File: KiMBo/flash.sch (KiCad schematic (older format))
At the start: 31 parts, among them IC1 24LC32AT-I/OT, U1 OSD3358, U5 74LVC1G06, U6 EMMC**G-S100

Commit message: More footprint association
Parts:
- IC1: footprint (none) -> TO_SOT_Packages_SMD:SOT-23-5
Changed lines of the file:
@@
 Connection ~ 12800 2650
 $Comp
-L GND #PWR092
+L GND #PWR093
 U 1 1 5893C2D6
 P 8300 4850
-F 0 "#PWR092" H 8300 4600 50  0001 C CNN
+F 0 "#PWR093" H 8300 4600 50  0001 C CNN
 F 1 "GND" H 8305 4677 50  0000 C CNN
 F 2 "" H 8300 4850 50  0000 C CNN
@@
 F 0 "IC1" H 12250 7018 50  0000 C CNN
 F 1 "24LC32AT-I/OT" H 12250 6927 50  0000 C CNN
-F 2 "" H 12250 6836 50  0001 C CIN
+F 2 "TO_SOT_Packages_SMD:SOT-23-5" H 12250 6836 50  0001 C CIN
 F 3 "" H 12250 6400 50  0000 C CNN
 	1    12250 6400
@@
 	11400 7000 11400 6950
 $Comp
-L GND #PWR093
+L GND #PWR094
 U 1 1 589CAA98
 P 12250 7050
-F 0 "#PWR093" H 12250 6800 50  0001 C CNN
+F 0 "#PWR094" H 12250 6800 50  0001 C CNN
 F 1 "GND" H 12255 6877 50  0000 C CNN
 F 2 "" H 12250 7050 50  0000 C CNN
@@
 $EndComp
 $Comp
-L GND #PWR094
+L GND #PWR095
 U 1 1 58ED63A5
 P 6750 7550
-F 0 "#PWR094" H 6750 7300 50  0001 C CNN
+F 0 "#PWR095" H 6750 7300 50  0001 C CNN
 F 1 "GND" H 6755 7377 50  0000 C CNN
 F 2 "" H 6750 7550 50  0000 C CNN
@@
 $EndComp
 $Comp
-L GND #PWR095
+L GND #PWR096
 U 1 1 58ED63B8
 P 6950 6900
-F 0 "#PWR095" H 6950 6650 50  0001 C CNN
+F 0 "#PWR096" H 6950 6650 50  0001 C CNN
 F 1 "GND" H 6955 6727 50  0000 C CNN
 F 2 "" H 6950 6900 50  0000 C CNN
@@
 $EndComp
 $Comp
-L GND #PWR096
+L GND #PWR097
 U 1 1 58ED63D4
 P 6450 8550
-F 0 "#PWR096" H 6450 8300 50  0001 C CNN
+F 0 "#PWR097" H 6450 8300 50  0001 C CNN
 F 1 "GND" H 6455 8377 50  0000 C CNN
 F 2 "" H 6450 8550 50  0000 C CNN
@@
 SERVO_0
 $Comp
-L VDD_3V3B #PWR097
+L VDD_3V3B #PWR098
 U 1 1 59E9BAE0
 P 10550 2600
-F 0 "#PWR097" H 10550 2450 50  0001 C CNN
+F 0 "#PWR098" H 10550 2450 50  0001 C CNN
 F 1 "VDD_3V3B" H 10565 2773 50  0000 C CNN
 F 2 "" H 10550 2600 50  0000 C CNN
@@
 USR0
 $Comp
-L VDD_3V3B #PWR098
+L VDD_3V3B #PWR099
 U 1 1 59FAFB00
 P 6450 8100
-F 0 "#PWR098" H 6450 7950 50  0001 C CNN
+F 0 "#PWR099" H 6450 7950 50  0001 C CNN
 F 1 "VDD_3V3B" H 6465 8273 50  0000 C CNN
 F 2 "" H 6450 8100 50  0000 C CNN
@@
 $EndComp
 $Comp
-L VDD_3V3B #PWR099
+L VDD_3V3B #PWR0100
 U 1 1 59FBC4DE
 P 6750 6450
-F 0 "#PWR099" H 6750 6300 50  0001 C CNN
+F 0 "#PWR0100" H 6750 6300 50  0001 C CNN
 F 1 "VDD_3V3B" H 6765 6623 50  0000 C CNN
 F 2 "" H 6750 6450 50  0000 C CNN
@@
 Connection ~ 11400 6600
 $Comp
-L VDD_3V3B #PWR0100
+L VDD_3V3B #PWR0101
 U 1 1 59FBD7EE
 P 11400 5950
-F 0 "#PWR0100" H 11400 5800 50  0001 C CNN
+F 0 "#PWR0101" H 11400 5800 50  0001 C CNN
 F 1 "VDD_3V3B" H 11415 6123 50  0000 C CNN
 F 2 "" H 11400 5950 50  0000 C CNN

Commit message: Create more footprints and add more associations
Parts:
- OSC1: footprint (none) -> KiMBo:Crystal_SMD_ASDMB_4Pads
- TP5: footprint (none) -> Measurement_Points:Measurement_Point_Round-SMD-Pad_Small
- U5: footprint (none) -> TO_SOT_Packages_SMD:SC-70-5
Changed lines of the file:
@@
 F 0 "U5" H 6450 7350 50  0000 L CNN
 F 1 "74LVC1G06" H 6800 7100 50  0000 L CNN
-F 2 "" H 6750 7200 50  0001 C CNN
+F 2 "TO_SOT_Packages_SMD:SC-70-5" H 6750 7200 50  0001 C CNN
 F 3 "" H 6750 7200 50  0000 C CNN
 	1    6750 7200
@@
 F 0 "OSC1" H 7050 8550 60  0000 C CNN
 F 1 "ASDMB" H 7050 8100 60  0000 C CNN
-F 2 "" H 7090 8260 60  0001 C CNN
+F 2 "KiMBo:Crystal_SMD_ASDMB_4Pads" H 7090 8260 60  0001 C CNN
 F 3 "" H 7090 8260 60  0001 C CNN
 	1    7050 8300
@@
 F 0 "TP5" H 11750 6750 50  0000 L CNN
 F 1 "Test_Point" H 11858 6579 50  0001 L CNN
-F 2 "" H 12000 6550 50  0001 C CNN
+F 2 "Measurement_Points:Measurement_Point_Round-SMD-Pad_Small" H 12000 6550 50  0001 C CNN
 F 3 "" H 12000 6550 50  0000 C CNN
 	1    11800 6550

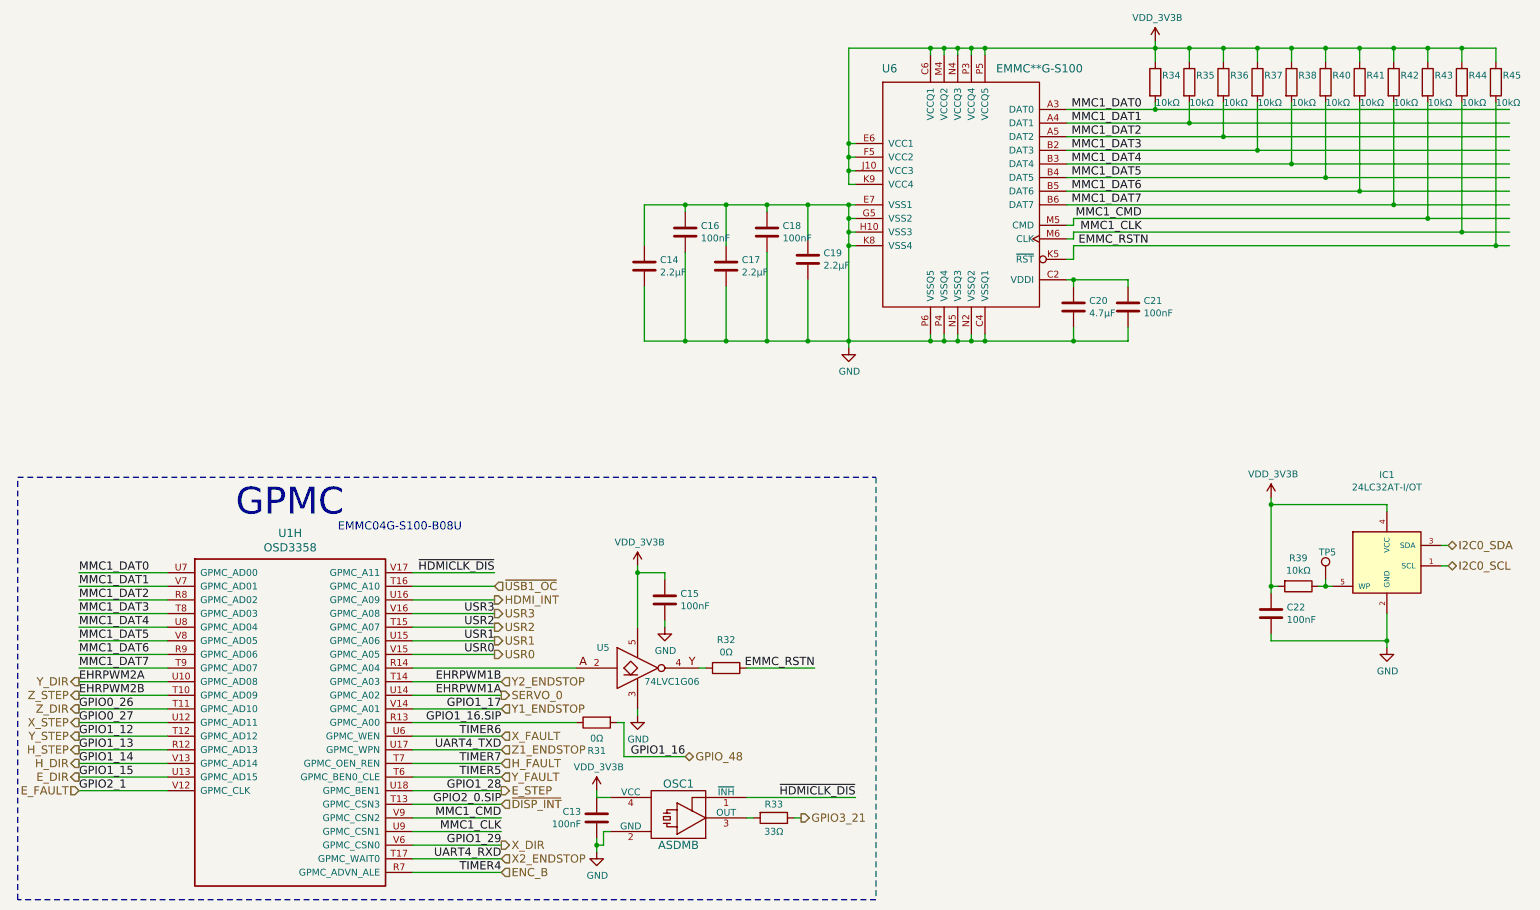
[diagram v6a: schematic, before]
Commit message: Begin layout
Arrange all connectors to get a feel for the area.
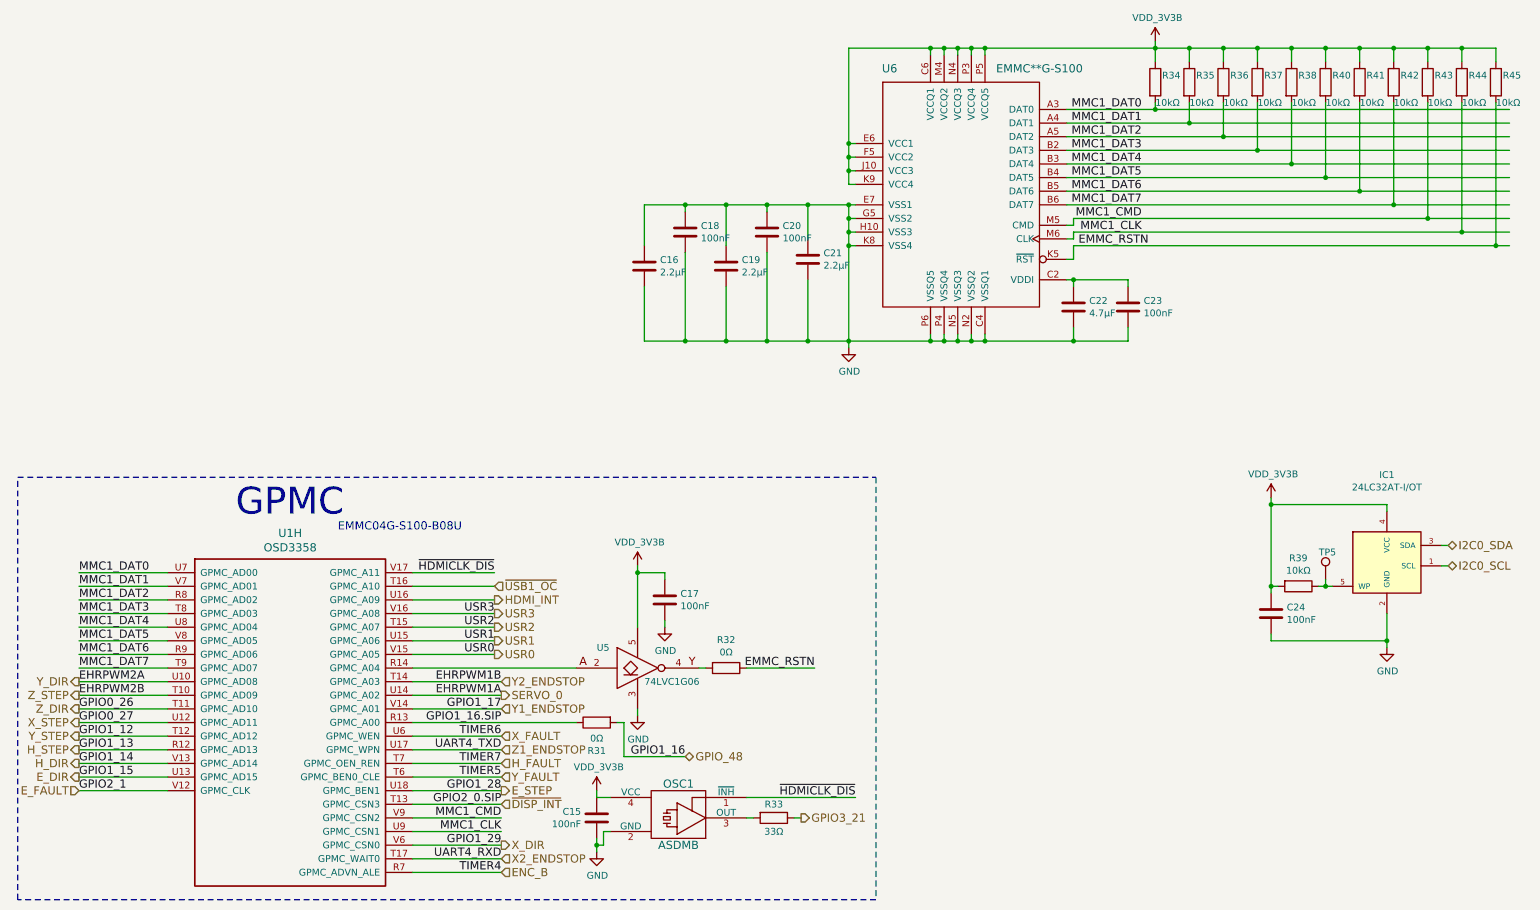
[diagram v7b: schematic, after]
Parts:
- renumbered C13 to C15, C14 to C16, C15 to C17, C16 to C18, C17 to C19, C18 to C20, C19 to C21, C20 to C22, C21 to C23, C22 to C24
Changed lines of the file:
@@
 Connection ~ 12800 2650
 $Comp
-L GND #PWR093
+L GND #PWR096
 U 1 1 5893C2D6
 P 8300 4850
-F 0 "#PWR093" H 8300 4600 50  0001 C CNN
+F 0 "#PWR096" H 8300 4600 50  0001 C CNN
 F 1 "GND" H 8305 4677 50  0000 C CNN
 F 2 "" H 8300 4850 50  0000 C CNN
@@
 Connection ~ 8300 4800
 $Comp
-L C C20
+L C C22
 U 1 1 5893CB56
 P 9950 4550
-F 0 "C20" H 10065 4596 50  0000 L CNN
+F 0 "C22" H 10065 4596 50  0000 L CNN
 F 1 "4.7μF" H 10065 4505 50  0000 L CNN
 F 2 "Capacitors_SMD:C_0805" H 9950 4550 50  0001 C CNN
@@
 $EndComp
 $Comp
-L C C21
+L C C23
 U 1 1 5893CB95
 P 10350 4550
-F 0 "C21" H 10465 4596 50  0000 L CNN
+F 0 "C23" H 10465 4596 50  0000 L CNN
 F 1 "100nF" H 10465 4505 50  0000 L CNN
 F 2 "Capacitors_SMD:C_0603" H 10350 4550 50  0001 C CNN
@@
 Connection ~ 9950 4350
 $Comp
-L C C19
+L C C21
 U 1 1 5893CF89
 P 8000 4200
-F 0 "C19" H 8115 4246 50  0000 L CNN
+F 0 "C21" H 8115 4246 50  0000 L CNN
 F 1 "2.2μF" H 8115 4155 50  0000 L CNN
 F 2 "Capacitors_SMD:C_0805" H 8000 4200 50  0001 C CNN
@@
 $EndComp
 $Comp
-L C C18
+L C C20
 U 1 1 5893D253
 P 7700 4000
-F 0 "C18" H 7815 4046 50  0000 L CNN
+F 0 "C20" H 7815 4046 50  0000 L CNN
 F 1 "100nF" H 7815 3955 50  0000 L CNN
 F 2 "Capacitors_SMD:C_0603" H 7700 4000 50  0001 C CNN
@@
 $EndComp
 $Comp
-L C C17
+L C C19
 U 1 1 5893D333
 P 7400 4250
-F 0 "C17" H 7515 4296 50  0000 L CNN
+F 0 "C19" H 7515 4296 50  0000 L CNN
 F 1 "2.2μF" H 7515 4205 50  0000 L CNN
 F 2 "Capacitors_SMD:C_0805" H 7400 4250 50  0001 C CNN
@@
 $EndComp
 $Comp
-L C C16
+L C C18
 U 1 1 5893D48C
 P 7100 4000
-F 0 "C16" H 7215 4046 50  0000 L CNN
+F 0 "C18" H 7215 4046 50  0000 L CNN
 F 1 "100nF" H 7215 3955 50  0000 L CNN
 F 2 "Capacitors_SMD:C_0603" H 7100 4000 50  0001 C CNN
@@
 $EndComp
 $Comp
-L C C14
+L C C16
 U 1 1 5893D4EE
 P 6800 4250
-F 0 "C14" H 6915 4296 50  0000 L CNN
+F 0 "C16" H 6915 4296 50  0000 L CNN
 F 1 "2.2μF" H 6915 4205 50  0000 L CNN
 F 2 "Capacitors_SMD:C_0805" H 6800 4250 50  0001 C CNN
@@
 	11400 6600 11450 6600
 $Comp
-L C C22
+L C C24
 U 1 1 589CA9AC
 P 11400 6800
-F 0 "C22" H 11515 6846 50  0000 L CNN
+F 0 "C24" H 11515 6846 50  0000 L CNN
 F 1 "100nF" H 11515 6755 50  0000 L CNN
 F 2 "Capacitors_SMD:C_0603" H 11400 6800 50  0001 C CNN
@@
 	11400 7000 11400 6950
 $Comp
-L GND #PWR094
+L GND #PWR097
 U 1 1 589CAA98
 P 12250 7050
-F 0 "#PWR094" H 12250 6800 50  0001 C CNN
+F 0 "#PWR097" H 12250 6800 50  0001 C CNN
 F 1 "GND" H 12255 6877 50  0000 C CNN
 F 2 "" H 12250 7050 50  0000 C CNN
@@
 $EndComp
 $Comp
-L GND #PWR095
+L GND #PWR098
 U 1 1 58ED63A5
 P 6750 7550
-F 0 "#PWR095" H 6750 7300 50  0001 C CNN
+F 0 "#PWR098" H 6750 7300 50  0001 C CNN
 F 1 "GND" H 6755 7377 50  0000 C CNN
 F 2 "" H 6750 7550 50  0000 C CNN
@@
 $EndComp
 $Comp
-L C C15
+L C C17
 U 1 1 58ED63B1
 P 6950 6700
-F 0 "C15" H 7065 6746 50  0000 L CNN
+F 0 "C17" H 7065 6746 50  0000 L CNN
 F 1 "100nF" H 7065 6655 50  0000 L CNN
 F 2 "Capacitors_SMD:C_0603" H 6988 6550 50  0001 C CNN
@@
 $EndComp
 $Comp
-L GND #PWR096
+L GND #PWR099
 U 1 1 58ED63B8
 P 6950 6900
-F 0 "#PWR096" H 6950 6650 50  0001 C CNN
+F 0 "#PWR099" H 6950 6650 50  0001 C CNN
 F 1 "GND" H 6955 6727 50  0000 C CNN
 F 2 "" H 6950 6900 50  0000 C CNN
@@
 $EndComp
 $Comp
-L C C13
+L C C15
 U 1 1 58ED63CD
 P 6450 8300
-F 0 "C13" H 6565 8346 50  0000 L CNN
+F 0 "C15" H 6565 8346 50  0000 L CNN
 F 1 "100nF" H 6565 8255 50  0000 L CNN
 F 2 "Capacitors_SMD:C_0603" H 6450 8300 50  0001 C CNN
@@
 $EndComp
 $Comp
-L GND #PWR097
+L GND #PWR0100
 U 1 1 58ED63D4
 P 6450 8550
-F 0 "#PWR097" H 6450 8300 50  0001 C CNN
+F 0 "#PWR0100" H 6450 8300 50  0001 C CNN
 F 1 "GND" H 6455 8377 50  0000 C CNN
 F 2 "" H 6450 8550 50  0000 C CNN
@@
 SERVO_0
 $Comp
-L VDD_3V3B #PWR098
+L VDD_3V3B #PWR0101
 U 1 1 59E9BAE0
 P 10550 2600
-F 0 "#PWR098" H 10550 2450 50  0001 C CNN
+F 0 "#PWR0101" H 10550 2450 50  0001 C CNN
 F 1 "VDD_3V3B" H 10565 2773 50  0000 C CNN
 F 2 "" H 10550 2600 50  0000 C CNN
@@
 USR0
 $Comp
-L VDD_3V3B #PWR099
+L VDD_3V3B #PWR0102
 U 1 1 59FAFB00
 P 6450 8100
-F 0 "#PWR099" H 6450 7950 50  0001 C CNN
+F 0 "#PWR0102" H 6450 7950 50  0001 C CNN
 F 1 "VDD_3V3B" H 6465 8273 50  0000 C CNN
 F 2 "" H 6450 8100 50  0000 C CNN
@@
 $EndComp
 $Comp
-L VDD_3V3B #PWR0100
+L VDD_3V3B #PWR0103
 U 1 1 59FBC4DE
 P 6750 6450
-F 0 "#PWR0100" H 6750 6300 50  0001 C CNN
+F 0 "#PWR0103" H 6750 6300 50  0001 C CNN
 F 1 "VDD_3V3B" H 6765 6623 50  0000 C CNN
 F 2 "" H 6750 6450 50  0000 C CNN
@@
 Connection ~ 11400 6600
 $Comp
-L VDD_3V3B #PWR0101
+L VDD_3V3B #PWR0104
 U 1 1 59FBD7EE
 P 11400 5950
-F 0 "#PWR0101" H 11400 5800 50  0001 C CNN
+F 0 "#PWR0104" H 11400 5800 50  0001 C CNN
 F 1 "VDD_3V3B" H 11415 6123 50  0000 C CNN
 F 2 "" H 11400 5950 50  0000 C CNN

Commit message: Remove HDMI from the schematic
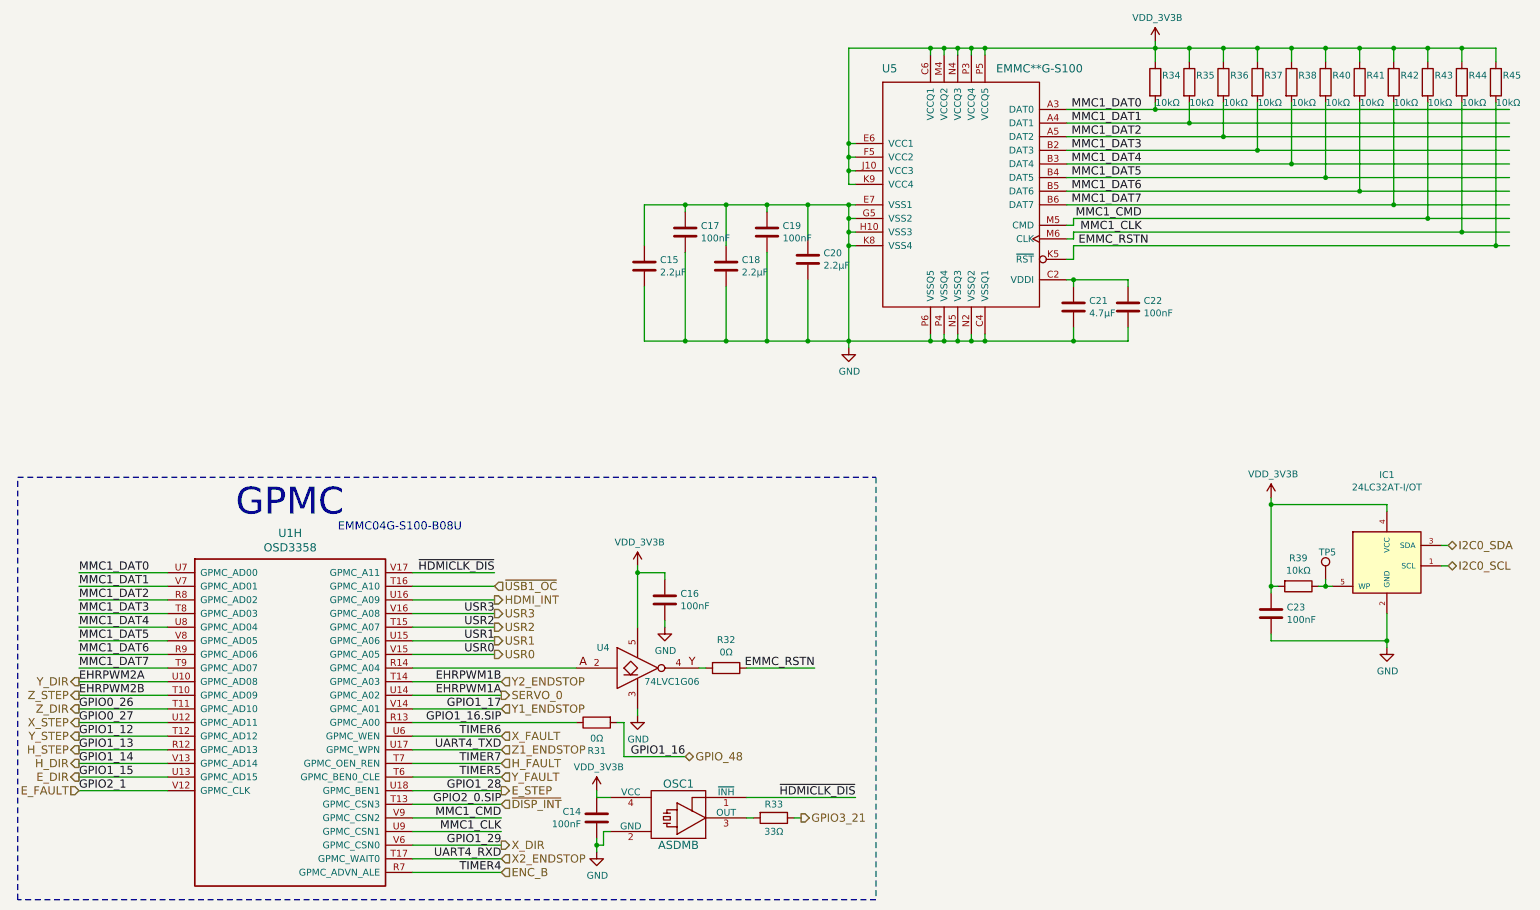
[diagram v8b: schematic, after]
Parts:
- renumbered C15 to C14, C16 to C15, C17 to C16, C18 to C17, C19 to C18, C20 to C19, C21 to C20, C22 to C21, C23 to C22, C24 to C23, U5 to U4, U6 to U5
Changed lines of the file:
@@
 $Descr A3 16535 11693
 encoding utf-8
-Sheet 6 26
+Sheet 6 25
 Title ""
 Date ""
@@
 Connection ~ 12800 2650
 $Comp
-L GND #PWR096
+L GND #PWR091
 U 1 1 5893C2D6
 P 8300 4850
-F 0 "#PWR096" H 8300 4600 50  0001 C CNN
+F 0 "#PWR091" H 8300 4600 50  0001 C CNN
 F 1 "GND" H 8305 4677 50  0000 C CNN
 F 2 "" H 8300 4850 50  0000 C CNN
@@
 Connection ~ 8300 4800
 $Comp
-L C C22
+L C C21
 U 1 1 5893CB56
 P 9950 4550
-F 0 "C22" H 10065 4596 50  0000 L CNN
+F 0 "C21" H 10065 4596 50  0000 L CNN
 F 1 "4.7μF" H 10065 4505 50  0000 L CNN
 F 2 "Capacitors_SMD:C_0805" H 9950 4550 50  0001 C CNN
@@
 $EndComp
 $Comp
-L C C23
+L C C22
 U 1 1 5893CB95
 P 10350 4550
-F 0 "C23" H 10465 4596 50  0000 L CNN
+F 0 "C22" H 10465 4596 50  0000 L CNN
 F 1 "100nF" H 10465 4505 50  0000 L CNN
 F 2 "Capacitors_SMD:C_0603" H 10350 4550 50  0001 C CNN
@@
 Connection ~ 9950 4350
 $Comp
-L C C21
+L C C20
 U 1 1 5893CF89
 P 8000 4200
-F 0 "C21" H 8115 4246 50  0000 L CNN
+F 0 "C20" H 8115 4246 50  0000 L CNN
 F 1 "2.2μF" H 8115 4155 50  0000 L CNN
 F 2 "Capacitors_SMD:C_0805" H 8000 4200 50  0001 C CNN
@@
 $EndComp
 $Comp
-L C C20
+L C C19
 U 1 1 5893D253
 P 7700 4000
-F 0 "C20" H 7815 4046 50  0000 L CNN
+F 0 "C19" H 7815 4046 50  0000 L CNN
 F 1 "100nF" H 7815 3955 50  0000 L CNN
 F 2 "Capacitors_SMD:C_0603" H 7700 4000 50  0001 C CNN
@@
 $EndComp
 $Comp
-L C C19
+L C C18
 U 1 1 5893D333
 P 7400 4250
-F 0 "C19" H 7515 4296 50  0000 L CNN
+F 0 "C18" H 7515 4296 50  0000 L CNN
 F 1 "2.2μF" H 7515 4205 50  0000 L CNN
 F 2 "Capacitors_SMD:C_0805" H 7400 4250 50  0001 C CNN
@@
 $EndComp
 $Comp
-L C C18
+L C C17
 U 1 1 5893D48C
 P 7100 4000
-F 0 "C18" H 7215 4046 50  0000 L CNN
+F 0 "C17" H 7215 4046 50  0000 L CNN
 F 1 "100nF" H 7215 3955 50  0000 L CNN
 F 2 "Capacitors_SMD:C_0603" H 7100 4000 50  0001 C CNN
@@
 $EndComp
 $Comp
-L C C16
+L C C15
 U 1 1 5893D4EE
 P 6800 4250
-F 0 "C16" H 6915 4296 50  0000 L CNN
+F 0 "C15" H 6915 4296 50  0000 L CNN
 F 1 "2.2μF" H 6915 4205 50  0000 L CNN
 F 2 "Capacitors_SMD:C_0805" H 6800 4250 50  0001 C CNN
@@
 	11400 6600 11450 6600
 $Comp
-L C C24
+L C C23
 U 1 1 589CA9AC
 P 11400 6800
-F 0 "C24" H 11515 6846 50  0000 L CNN
+F 0 "C23" H 11515 6846 50  0000 L CNN
 F 1 "100nF" H 11515 6755 50  0000 L CNN
 F 2 "Capacitors_SMD:C_0603" H 11400 6800 50  0001 C CNN
@@
 	11400 7000 11400 6950
 $Comp
-L GND #PWR097
+L GND #PWR092
 U 1 1 589CAA98
 P 12250 7050
-F 0 "#PWR097" H 12250 6800 50  0001 C CNN
+F 0 "#PWR092" H 12250 6800 50  0001 C CNN
 F 1 "GND" H 12255 6877 50  0000 C CNN
 F 2 "" H 12250 7050 50  0000 C CNN
@@
 GPIO2_0.SIP
 $Comp
-L 74LVC1G06 U5
+L 74LVC1G06 U4
 U 1 1 58ED639E
 P 6750 7200
-F 0 "U5" H 6450 7350 50  0000 L CNN
+F 0 "U4" H 6450 7350 50  0000 L CNN
 F 1 "74LVC1G06" H 6800 7100 50  0000 L CNN
 F 2 "TO_SOT_Packages_SMD:SC-70-5" H 6750 7200 50  0001 C CNN
@@
 $EndComp
 $Comp
-L GND #PWR098
+L GND #PWR093
 U 1 1 58ED63A5
 P 6750 7550
-F 0 "#PWR098" H 6750 7300 50  0001 C CNN
+F 0 "#PWR093" H 6750 7300 50  0001 C CNN
 F 1 "GND" H 6755 7377 50  0000 C CNN
 F 2 "" H 6750 7550 50  0000 C CNN
@@
 $EndComp
 $Comp
-L C C17
+L C C16
 U 1 1 58ED63B1
 P 6950 6700
-F 0 "C17" H 7065 6746 50  0000 L CNN
+F 0 "C16" H 7065 6746 50  0000 L CNN
 F 1 "100nF" H 7065 6655 50  0000 L CNN
 F 2 "Capacitors_SMD:C_0603" H 6988 6550 50  0001 C CNN
@@
 $EndComp
 $Comp
-L GND #PWR099
+L GND #PWR094
 U 1 1 58ED63B8
 P 6950 6900
-F 0 "#PWR099" H 6950 6650 50  0001 C CNN
+F 0 "#PWR094" H 6950 6650 50  0001 C CNN
 F 1 "GND" H 6955 6727 50  0000 C CNN
 F 2 "" H 6950 6900 50  0000 C CNN
@@
 $EndComp
 $Comp
-L C C15
+L C C14
 U 1 1 58ED63CD
 P 6450 8300
-F 0 "C15" H 6565 8346 50  0000 L CNN
+F 0 "C14" H 6565 8346 50  0000 L CNN
 F 1 "100nF" H 6565 8255 50  0000 L CNN
 F 2 "Capacitors_SMD:C_0603" H 6450 8300 50  0001 C CNN
@@
 $EndComp
 $Comp
-L GND #PWR0100
+L GND #PWR095
 U 1 1 58ED63D4
 P 6450 8550
-F 0 "#PWR0100" H 6450 8300 50  0001 C CNN
+F 0 "#PWR095" H 6450 8300 50  0001 C CNN
 F 1 "GND" H 6455 8377 50  0000 C CNN
 F 2 "" H 6450 8550 50  0000 C CNN
@@
 MMC1_CLK
 $Comp
-L EMMC**G-S100 U6
+L EMMC**G-S100 U5
 U 1 1 5893814B
 P 9150 3750
-F 0 "U6" H 8600 4700 60  0000 C CNN
+F 0 "U5" H 8600 4700 60  0000 C CNN
 F 1 "EMMC**G-S100" H 9700 4700 60  0000 C CNN
 F 2 "KiMBo:EMMCxxG-S100" H 9150 4250 60  0001 C CNN
@@
 SERVO_0
 $Comp
-L VDD_3V3B #PWR0101
+L VDD_3V3B #PWR096
 U 1 1 59E9BAE0
 P 10550 2600
-F 0 "#PWR0101" H 10550 2450 50  0001 C CNN
+F 0 "#PWR096" H 10550 2450 50  0001 C CNN
 F 1 "VDD_3V3B" H 10565 2773 50  0000 C CNN
 F 2 "" H 10550 2600 50  0000 C CNN
@@
 USR0
 $Comp
-L VDD_3V3B #PWR0102
+L VDD_3V3B #PWR097
 U 1 1 59FAFB00
 P 6450 8100
-F 0 "#PWR0102" H 6450 7950 50  0001 C CNN
+F 0 "#PWR097" H 6450 7950 50  0001 C CNN
 F 1 "VDD_3V3B" H 6465 8273 50  0000 C CNN
 F 2 "" H 6450 8100 50  0000 C CNN
@@
 $EndComp
 $Comp
-L VDD_3V3B #PWR0103
+L VDD_3V3B #PWR098
 U 1 1 59FBC4DE
 P 6750 6450
-F 0 "#PWR0103" H 6750 6300 50  0001 C CNN
+F 0 "#PWR098" H 6750 6300 50  0001 C CNN
 F 1 "VDD_3V3B" H 6765 6623 50  0000 C CNN
 F 2 "" H 6750 6450 50  0000 C CNN
@@
 Connection ~ 11400 6600
 $Comp
-L VDD_3V3B #PWR0104
+L VDD_3V3B #PWR099
 U 1 1 59FBD7EE
 P 11400 5950
-F 0 "#PWR0104" H 11400 5800 50  0001 C CNN
+F 0 "#PWR099" H 11400 5800 50  0001 C CNN
 F 1 "VDD_3V3B" H 11415 6123 50  0000 C CNN
 F 2 "" H 11400 5950 50  0000 C CNN
